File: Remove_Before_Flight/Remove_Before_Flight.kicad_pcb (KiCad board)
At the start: 2 copper layers, 80 x 20 mm, 2 parts, among them J1 Conn_02x03_Counter_Clockwise, J2 Conn_02x03_Counter_Clockwise

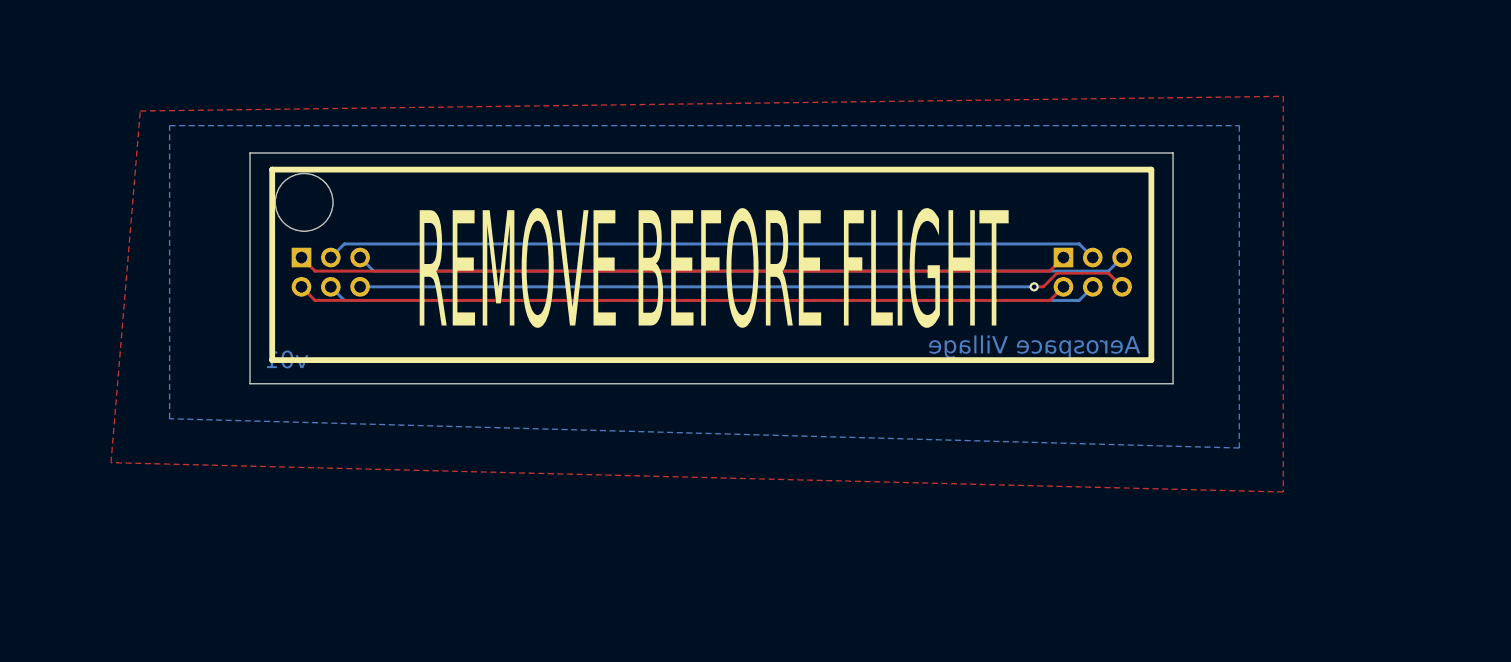
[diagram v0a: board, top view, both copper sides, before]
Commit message: updated remove before flight to v02
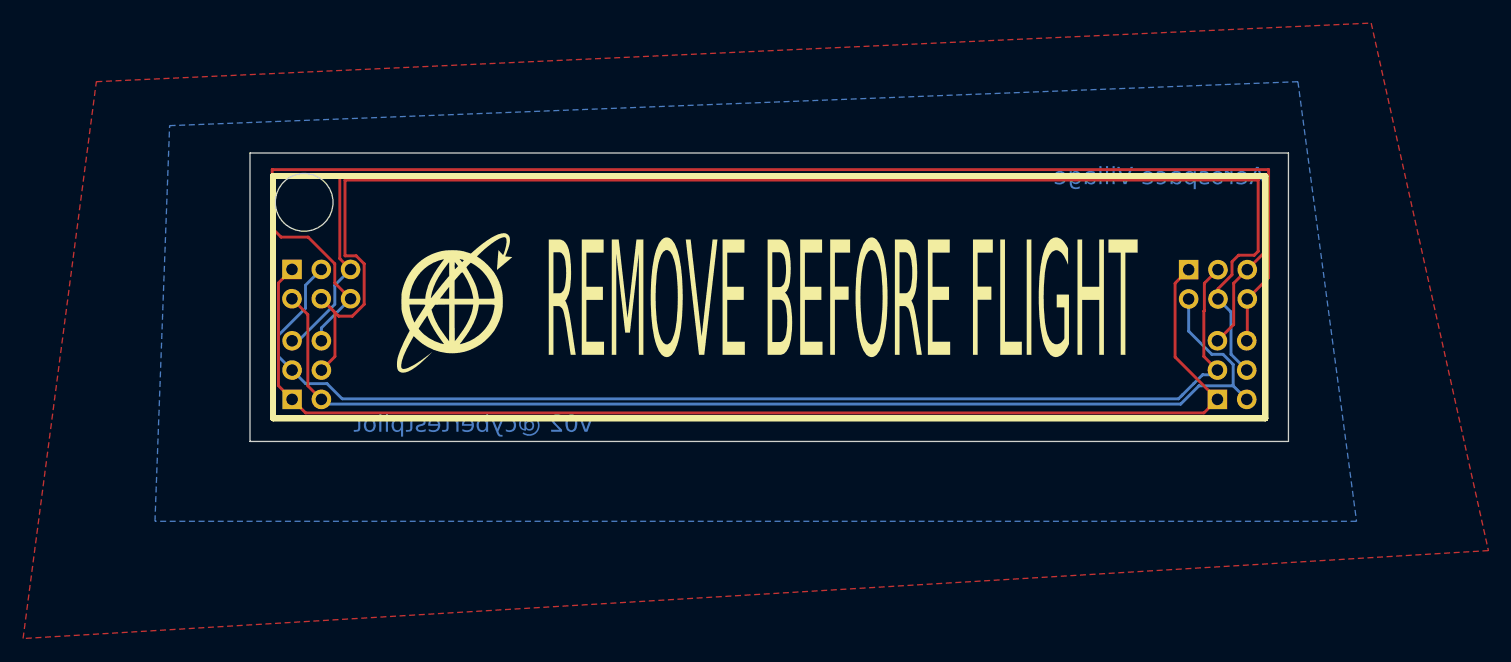
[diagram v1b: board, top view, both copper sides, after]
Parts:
- added J3: Conn_02x03_Counter_Clockwise, Connector_PinHeader_2.54mm:PinHeader_2x03_P2.54mm_Vertical, B.Cu at (123.6, 111.4)
- added J4: Conn_02x03_Counter_Clockwise, Connector_PinHeader_2.54mm:PinHeader_2x03_P2.54mm_Vertical, B.Cu at (203.8, 111.4)
- added svg2mod: G***, aerospace_badge:aerospace_logo_new, F.Cu at (136.6, 101.4)
- added svg2mod: G***, aerospace_badge:aerospace_logo_new, B.Cu at (195.0, 101.1)
- moved J2 10.9 mm to (201.4, 100.1)
- moved J1 1.32 mm to (123.6, 100.1)
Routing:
- net Net-(J1-Pad4): track 67.0 -> 122.8 mm
- net Net-(J1-Pad6): track 67.0 -> 122.0 mm, vias 1 -> 0
- net Net-(J1-Pad5): track 67.0 -> 113.3 mm
- net Net-(J1-Pad1): track 67.0 -> 106.7 mm
- net Net-(J1-Pad3): track 67.0 -> 102.9 mm
- net Net-(J1-Pad2): track 67.0 -> 101.0 mm
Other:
- board size 80 x 20 mm -> 90 x 25 mm
- board text added: "v02 @cybertestpilot"
- board text removed: "v01"
